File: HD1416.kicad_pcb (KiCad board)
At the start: 2 copper layers, 97.8 x 97.8 mm, 39 parts, among them J1 AudioJack2, Q1 MPSA20, Q2 MPSA20, Q3 BC547A

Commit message: Fixed pcb new and sch
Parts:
- moved H11 0.64 mm to (43.2, 159.4)
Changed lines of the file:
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@@
   )
   (footprint "Connector_Wire:SolderWire-0.5sqmm_1x01_D0.9mm_OD2.3mm" (layer "F.Cu")
-    (at 43.18 160.02)
+    (at 43.18 159.385)
     (descr "Soldered wire connection, for a single 0.5 mm² wire, reinforced insulation, conductor diameter 0.9mm, outer diameter 2.3mm, size source Multi-Contact FLEXI-xV 0.5 (https://ec.staubli.com/AcroFiles/Catalogues/TM_Cab-Main-11014119_(en)_hi.pdf), bend radius 3 times outer diameter, generated with kicad-footprint-generator")
     (tags "connector wire 0.5sqmm")

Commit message: routing board and improving 3D
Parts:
- C2: footprint Capacitor_THT:C_Rect_L9.0mm_W2.5mm_P7.50mm_MKT -> footprints:C315C103K5R5TA7303
- J1: value AudioJack2 -> Audio Jack
- Spkr: renamed from LS1; footprint Buzzer_Beeper:Speaker_CUI_CMR-1206S-67 -> Connector_Wire:SolderWire-0.5sqmm_1x02_P4.8mm_D0.9mm_OD2.3mm
- moved C2 8.94 mm to (68.6, 109.0)
- moved V1 1.09 mm to (71.9, 117.6)
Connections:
- net +9 renamed VCC
- net /node5 renamed Net-(C2-Pad2)
- net /node6 renamed Net-(C3-Pad2)
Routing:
- net VCC: track 0.00 -> 117.2 mm
- net /astable2: track 0.00 -> 37.4 mm
- net /astable1: track 0.00 -> 31.2 mm
- net Net-(C3-Pad2): track 0.00 -> 30.9 mm
- net Net-(C5-Pad1): track 0.00 -> 30.5 mm
- net Net-(C2-Pad2): track 0.00 -> 28.2 mm
- net Net-(C5-Pad2): track 0.00 -> 26.0 mm
- net /speaker: track 0.00 -> 20.8 mm
- net Net-(H3-Pad1): track 0.00 -> 18.5 mm
- net Net-(C1-Pad2): track 0.00 -> 12.7 mm
- net Net-(R3-Pad2): track 0.00 -> 9.56 mm
- net Net-(C1-Pad1): track 0.00 -> 5.12 mm
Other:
- board text added: "+"

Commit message: improved sch pcb 3d
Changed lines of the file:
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@@
     (pad "3" thru_hole circle locked (at 5.08 0) (size 1.27 1.27) (drill 0.762) (layers *.Cu *.Mask)
       (net 2 "GND") (pinfunction "3") (pintype "passive"))
+    (model "${KIPRJMOD}/3D Models/3299X.stp"
+      (offset (xyz 0 0 0))
+      (scale (xyz 1 1 1))
+      (rotate (xyz 0 0 0))
+    )
   )
   (footprint "TestPoint:TestPoint_Pad_D2.0mm" (layer "F.Cu")
@@
     (property "Sheetname" "")
     (attr through_hole)
-    (fp_text reference "C2" (at 1.27 0 -90) (layer "F.SilkS")
-      (effects (font (size 1 1) (thickness 0.15)))
-    )
-    (fp_text value ".005u" (at 1.27 0 -90) (layer "F.SilkS")
+    (fp_text reference "C2" (at 1.27 2.286 -90) (layer "F.SilkS")
+      (effects (font (size 1 1) (thickness 0.15)))
+    )
+    (fp_text value ".005u" (at 1.27 -2.286 -90) (layer "F.SilkS")
       (effects (font (size 1 1) (thickness 0.15)))
     )
@@
       (net 4 "Net-(C2-Pad2)") (pintype "passive"))
     (model "${KIPRJMOD}/3D Models/C315C103K5R5TA7303.step"
-      (offset (xyz -0.5 -1 0.5))
-      (scale (xyz 1 1 1))
-      (rotate (xyz -90 0 -180))
-    )
-  )
+      (offset (xyz 0 0 0))
+      (scale (xyz 1 1 1))
+      (rotate (xyz 0 0 0))
+    )
+  )

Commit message: updated modeling
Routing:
- net GND: track 0.00 -> 171.1 mm
- net Net-(C4-Pad2): track 0.00 -> 28.6 mm
- net VCC: track 117.2 -> 99.8 mm
- net Net-(C5-Pad1): track 30.5 -> 44.3 mm
- net Net-(C2-Pad2): track 28.2 -> 39.7 mm
- net Net-(C5-Pad2): track 26.0 -> 35.3 mm
- net /astable1: track 31.2 -> 27.5 mm
- net Net-(R3-Pad2): track 9.56 -> 7.88 mm
- net /astable2: track 37.4 -> 35.8 mm
- net /speaker: track 20.8 -> 19.3 mm
- net Net-(H3-Pad1): track 18.5 -> 17.7 mm
- net Net-(C3-Pad2): track 30.9 -> 31.6 mm
- added copper zone on B.Cu, net GND
- added copper zone on F.Cu, net GND

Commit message: catching up on all changes
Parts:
- removed J1: Audio Jack, Connector_Wire:SolderWire-0.5sqmm_1x02_P4.8mm_D0.9mm_OD2.3mm
- renumbered Spkr to LS1
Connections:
- H3 pad 1: Net-(H3-Pad1) -> Net-(C5-Pad1)
- R9 pad 2: Net-(H3-Pad1) -> Net-(C5-Pad1)
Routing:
- net Net-(H3-Pad1): track 17.7 -> 0.00 mm
- net Net-(C5-Pad1): track 44.3 -> 54.5 mm
- net GND: track 171.1 -> 169.3 mm
- net Net-(C3-Pad2): track 31.6 -> 30.1 mm
- net /speaker: track 19.3 -> 20.1 mm
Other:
- board text removed: "S"
- board text removed: "T"

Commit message: updates to kicad 8.0
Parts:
- H3: value 8200 -> type="R" model="8200" lib=""
- H4: value F -> type="R" model="F" lib=""
- H5: value E -> type="R" model="E" lib=""
- H6: value D -> type="R" model="D" lib=""
- H7: value C -> type="R" model="C" lib=""
- H8: value B -> type="R" model="B" lib=""
- TP1: value 2.4 -> type="R" model="2.4" lib=""
- TP2: value -0.3 -> type="R" model="-0.3" lib=""
- TP3: value -2.1 -> type="R" model="-2.1" lib=""
- TP4: value 5.1 -> type="R" model="5.1" lib=""
- TP5: value 0.5 -> type="R" model="0.5" lib=""
- TP6: value 7.5 -> type="R" model="7.5" lib=""
- renumbered H9 to J2
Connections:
- C1 pad 1: Net-(C1-Pad1) -> GND
- C1 pad 2: Net-(C1-Pad2) -> Net-(D1-A)
- D1 pad 2: Net-(C1-Pad1) -> Net-(D1-A)
- J2 pad 1: Net-(C1-Pad2) -> Net-(D1-A)
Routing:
- net Net-(C1-Pad1): track 5.12 -> 0.00 mm
- net GND: track 169.3 -> 174.5 mm

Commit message: updates to schematic
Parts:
- H3: value type="R" model="8200" lib="" -> "8200"
- H4: value type="R" model="F" lib="" -> "E"
- H5: value type="R" model="E" lib="" -> "F"
- H6: value type="R" model="D" lib="" -> "D"
- H7: value type="R" model="C" lib="" -> "C"
- H8: value type="R" model="B" lib="" -> "B"
- TP1: value type="R" model="2.4" lib="" -> "2.4"
- TP2: value type="R" model="-0.3" lib="" -> "-0.3"
- TP3: value type="R" model="-2.1" lib="" -> "-2.1"
- TP4: value type="R" model="5.1" lib="" -> "5.1"
- TP5: value type="R" model="0.5" lib="" -> "0.5"
- TP6: value type="R" model="7.5" lib="" -> "7.5"
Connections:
- C5 pad 1: Net-(C5-Pad1) -> Net-(H4-Pin_1)
- H3 pad 1: Net-(C5-Pad1) -> Net-(H3-Pin_1)
- H4 pad 1: Net-(C5-Pad1) -> Net-(H4-Pin_1)
- H5 pad 1: Net-(C5-Pad1) -> Net-(H4-Pin_1)
- H7 pad 1: Net-(C5-Pad1) -> Net-(H4-Pin_1)
- R9 pad 2: Net-(C5-Pad1) -> Net-(H3-Pin_1)
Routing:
- net Net-(C5-Pad1): track 54.5 -> 0.00 mm
- net (no net): track 0.00 -> 54.5 mm

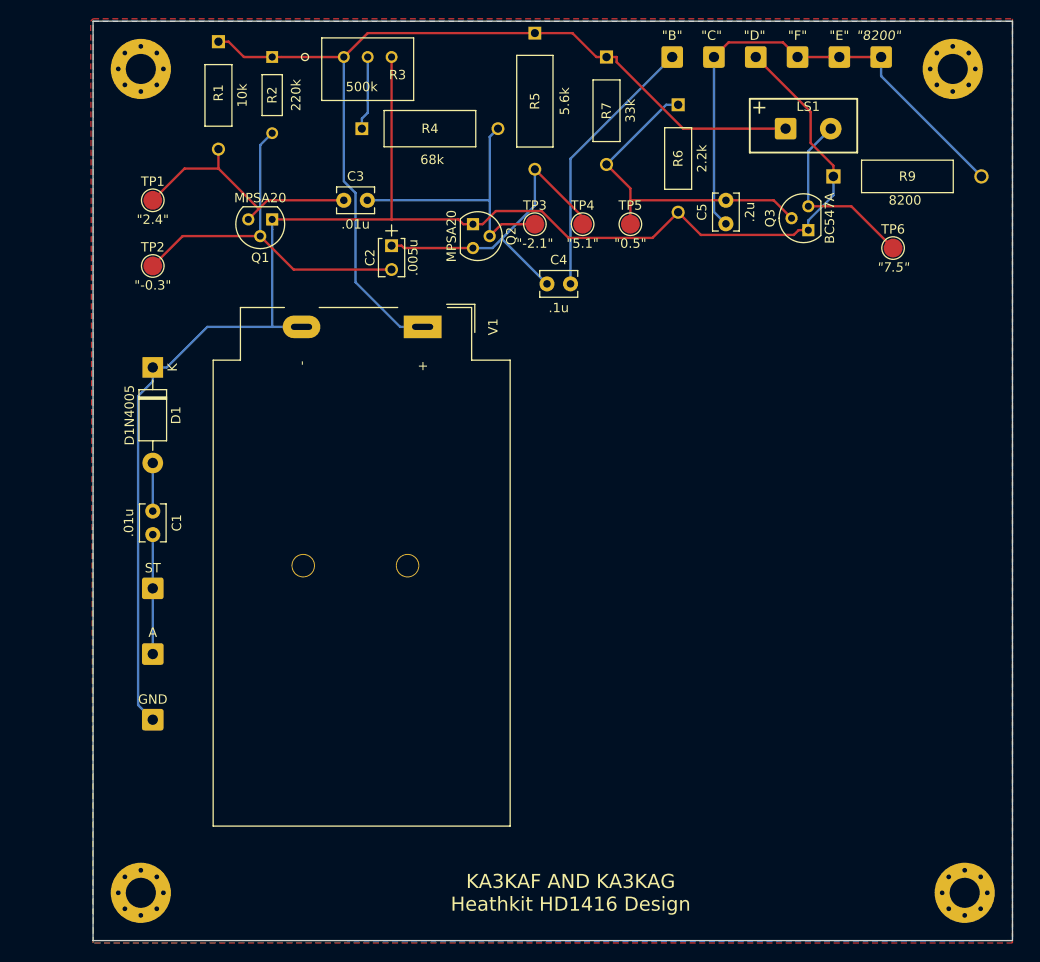
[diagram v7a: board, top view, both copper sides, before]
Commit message: updates to audio jack
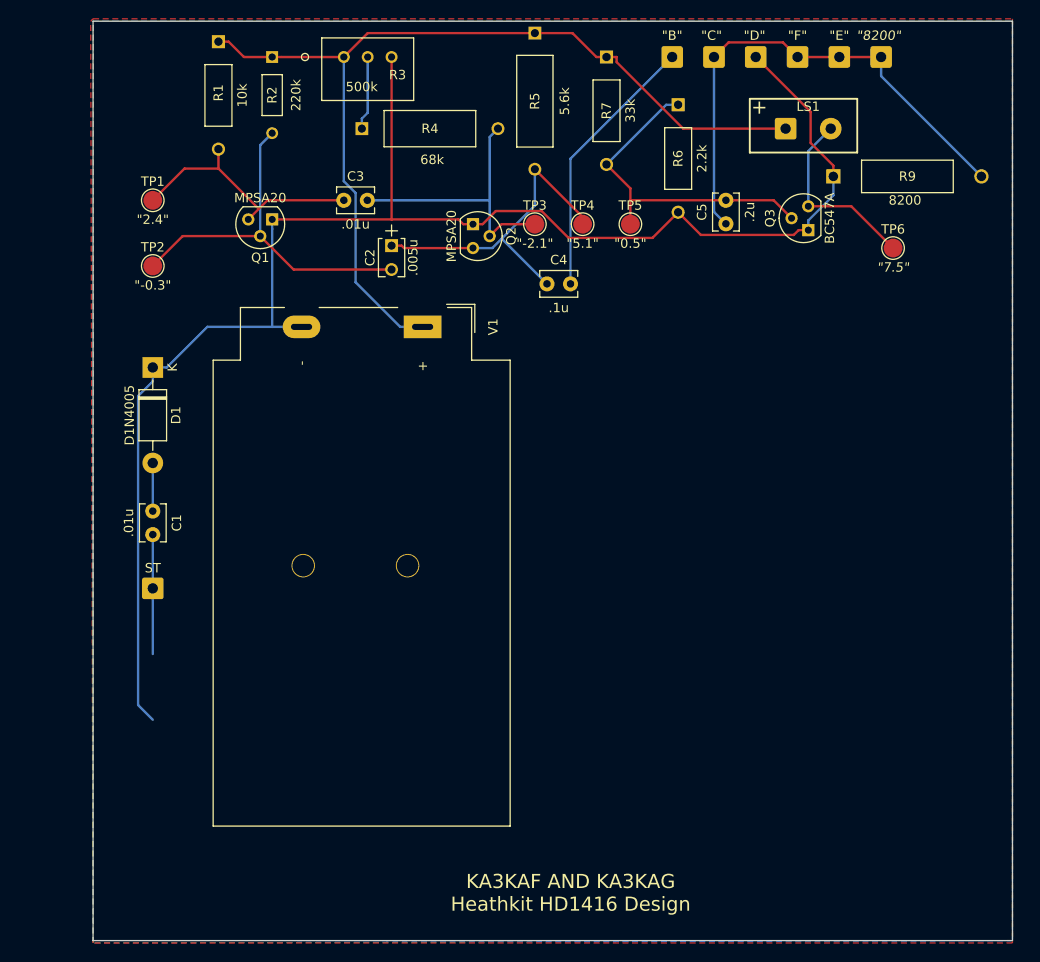
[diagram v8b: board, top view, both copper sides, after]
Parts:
- removed H10: A, Connector_Wire:SolderWire-0.5sqmm_1x01_D0.9mm_OD2.3mm
- removed H11: GND, Connector_Wire:SolderWire-0.5sqmm_1x01_D0.9mm_OD2.3mm
- removed REF1, REF2, REF3, REF4: MountingHole_3.2mm_M3_Pad_Via, MountingHole:MountingHole_3.2mm_M3_Pad_Via
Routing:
- net Net-(D1-A): track 0.00 -> 12.7 mm
- net Net-(C1-Pad2): track 12.7 -> 0.00 mm
